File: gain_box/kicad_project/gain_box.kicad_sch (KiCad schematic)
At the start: 120 parts, among them J1 Conn_01x02, J10 AVR-UPDI-6, J11 Conn_01x02, J2 Conn_01x02, J3 Conn_01x02, J4 Conn_01x02, J5 Conn_01x02, J6 Conn_01x02, J7 Conn_01x02, J8 Conn_01x02, J9 Conn_01x02, K1 J104D2C12VDC.36S, K2 J104D2C12VDC.36S, K3 G5V-1, K4 J107F1CS2012VDC.80, K5 J104D2C12VDC.36S, Q1 AO3400A, Q2 AO3400A, Q3 AO3400A, T1 70042K, U1 NE5532, U10 140817141310, U2 NE5532, U3 NE5532, U4 LM7809, U5 LM7909, U6 78L05, U7 ATtiny412-SS, U9 140817141310

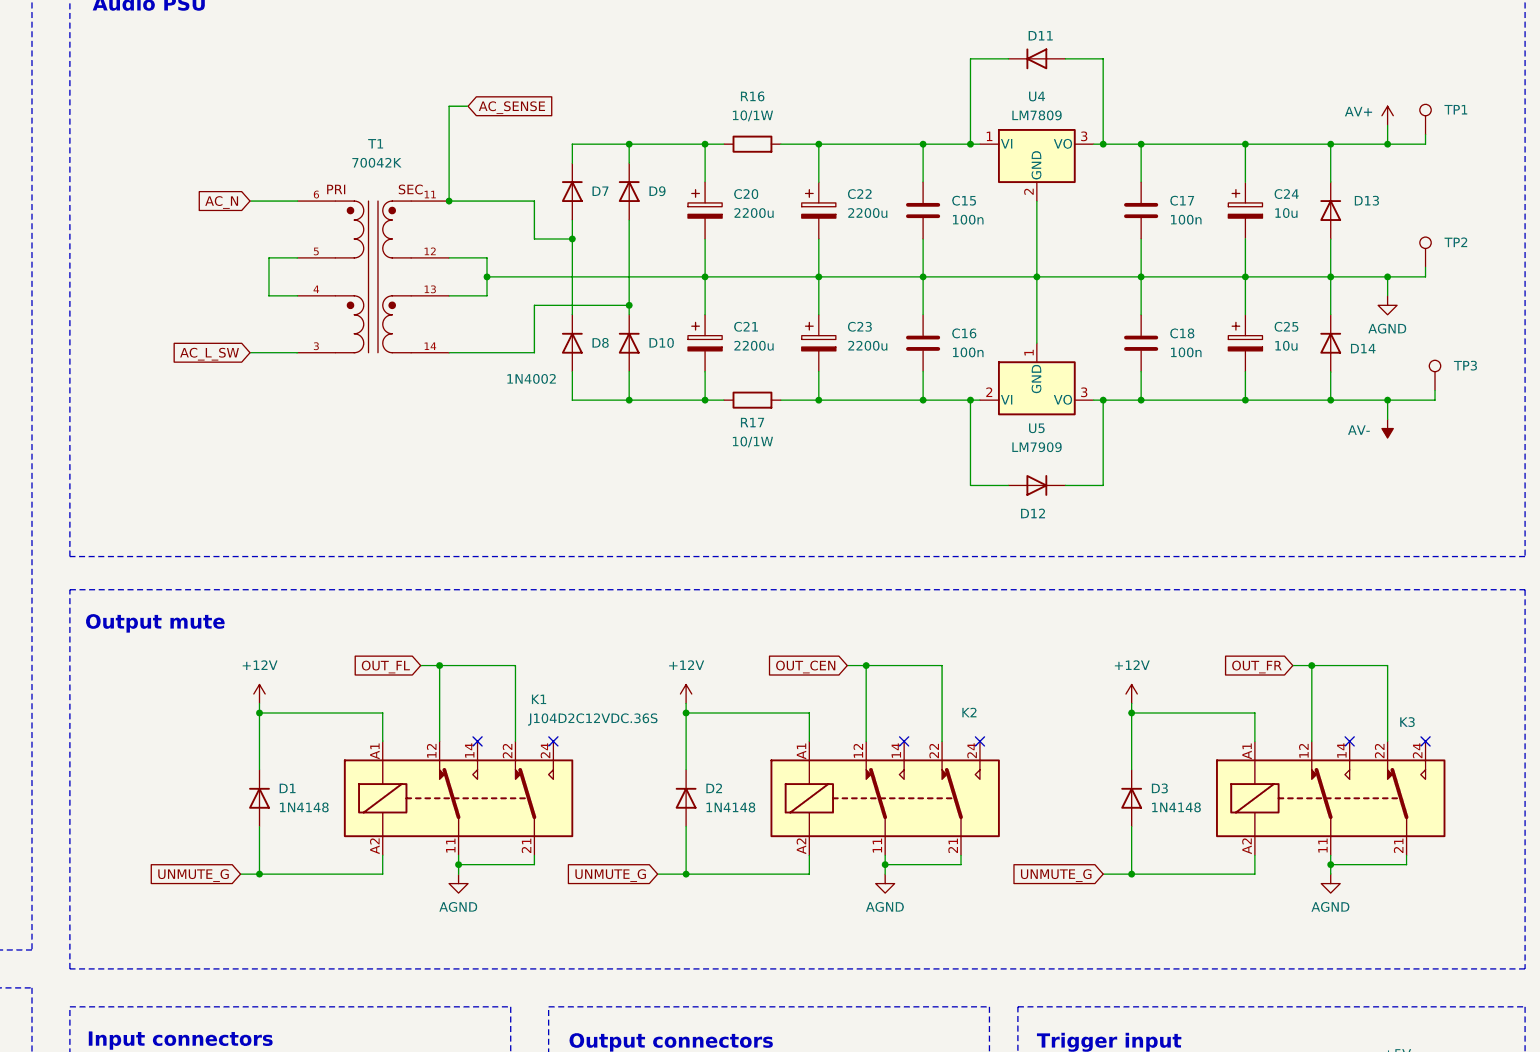
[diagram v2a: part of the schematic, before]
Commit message: gain_box new PSU position
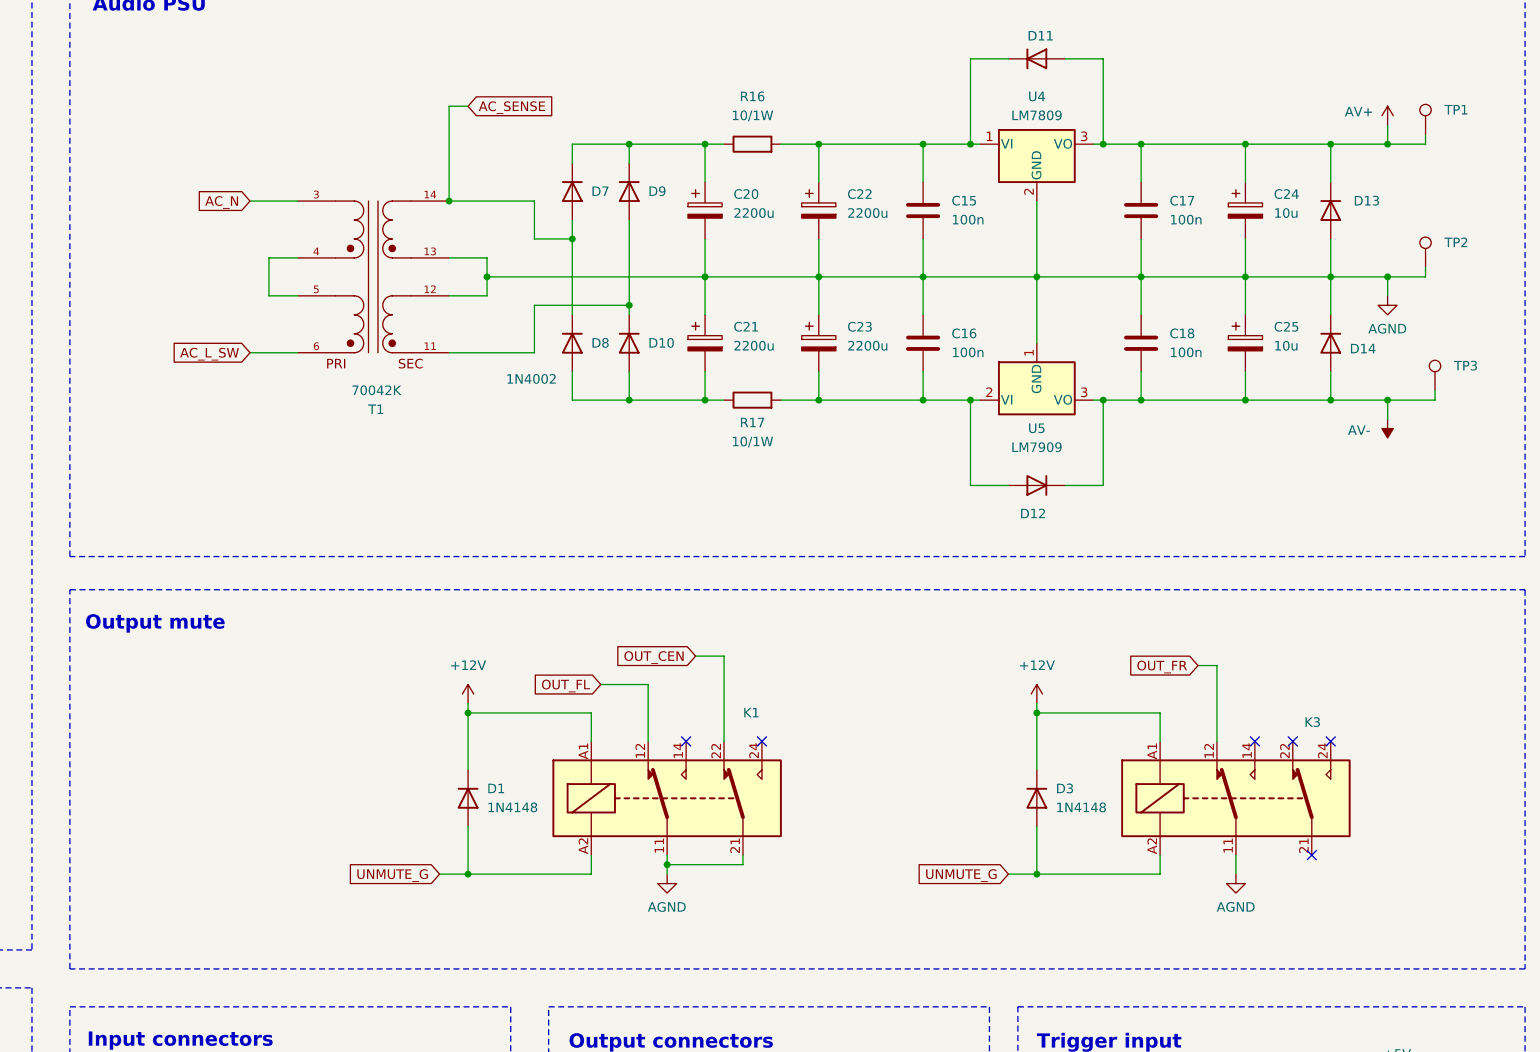
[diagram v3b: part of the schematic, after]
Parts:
- removed D1: 1N4148, Diode_THT:D_DO-35_SOD27_P7.62mm_Horizontal, symbol Device:D
- removed K1: J104D2C12VDC.36S, Relay_THT:Relay_DPDT_Finder_30.22, symbol Relay:FINDER-30.22
- renumbered D2 to D1, K2 to K1
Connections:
- net AC_L_SW: now also T1.6; no longer T1.3
- net AC_N: now also T1.3; no longer T1.6
- net AC_SENSE: now also T1.14; no longer T1.11
- net AGND: no longer K3.21
- net OUT_CEN: no longer K1.12
- net OUT_FL: now also K1.12
- net OUT_FR: no longer K3.22
- net at D10.1 (K), D9.2 (A): now also T1.11; no longer T1.14
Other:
- moved on the sheet: D1, D3, K1, K3, T1

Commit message: update
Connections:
- net +12V: no longer K5.11
- net TGO2: no longer K5.14
- no-connect marks 8 -> 9
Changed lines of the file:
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@@
 	)
 	(junction
-		(at 26.67 234.95)
-		(diameter 0)
-		(color 0 0 0 0)
-	)
-	(junction
 		(at 384.81 74.93)
 		(diameter 0)
@@
 	)
 	(no_connect
+		(at 48.26 232.41)
+	)
+	(no_connect
 		(at 377.19 120.65)
 	)
@@
 	(wire
 		(pts
-			(xy 48.26 232.41) (xy 52.07 232.41)
-		)
-		(stroke
-			(width 0)
-			(type default)
-		)
-	)
-	(wire
-		(pts
 			(xy 76.2 41.91) (xy 80.01 41.91)
 		)
@@
 	(wire
 		(pts
-			(xy 26.67 224.79) (xy 26.67 234.95)
+			(xy 26.67 224.79) (xy 26.67 245.11)
 		)
 		(stroke
@@
 	(wire
 		(pts
-			(xy 26.67 234.95) (xy 33.02 234.95)
-		)
-		(stroke
-			(width 0)
-			(type default)
-		)
-	)
-	(wire
-		(pts
 			(xy 76.2 83.82) (xy 80.01 83.82)
 		)
@@
 	(wire
 		(pts
-			(xy 26.67 234.95) (xy 26.67 245.11)
-		)
-		(stroke
-			(width 0)
-			(type default)
-		)
-	)
-	(wire
-		(pts
 			(xy 361.95 236.22) (xy 364.49 236.22)
 		)
@@
 			(effects
 				(font
-					(size 1.27 1.27)
-				)
-				(justify left)
-				(hide yes)
-			)
-		)
-	)
-	(global_label "TGO2"
-		(shape input)
-		(at 52.07 232.41 0)
-		(effects
-			(font
-				(size 1.27 1.27)
-			)
-			(justify left)
-		)
-		(property "Intersheetrefs" "${INTERSHEET_REFS}"
-			(at 43.2019 229.87 0)
-			(effects
-				(font
